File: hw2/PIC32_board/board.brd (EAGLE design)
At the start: 50 x 50 mm, 22 parts, among them J1 USB-MB-H

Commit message: Complete board design, add PCB gerber files.
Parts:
- removed V_REG(3.3V): MCP1702, me433:TO-92
- added U$1: SOT-223, me433:NU32V7_SOT223
- C1, C5: device me433:CT6032 -> me433:CAP-POL-0603
- C2, C3, C4, C7: device rcl:C1206 -> resistor:C0603
- CLOCK: value OSCO -> OSC; device me433:OSC -> me433:NU32V7_RESONATOR-SMD
- GREEN: value (none) -> GREEN; device led:LED3MM -> me433:LED-0603
- J1: value USB-MB-H -> USB; device me433:USB-MB-H -> me433:NU32V7_USB-MINIB
- R1, R2, R3, R4: device resistor:R1206 -> resistor:R0603
- RED: value (none) -> RED; device led:LED3MM -> me433:LED-0603
- RESET, USER: device me433:PUSH -> me433:NU32V7_MOM_SW
- moved SWITCH 44.3 mm to (47.6, 41.1), turned to 270 degrees
- moved CONN2 38.7 mm to (48.9, 16.5), turned to 90 degrees
- moved R1 37.7 mm to (48.3, 4.24), turned to 270 degrees
- moved R3 37.1 mm to (42.1, 42.2), turned to 0 degrees
- moved J1 36.3 mm to (6.49, 43.7), turned to 270 degrees
- moved C3 35.1 mm to (31.6, 38.0), turned to 270 degrees
- moved RED 35.1 mm to (38.0, 1.36), turned to 0 degrees
- moved R4 33.8 mm to (24.8, 43.4), turned to 0 degrees
- moved GREEN 33.6 mm to (31.8, 1.46), turned to 180 degrees
- moved RESET 32.8 mm to (39.6, 47.2), turned to 0 degrees
- moved CONN1 31.9 mm to (1.27, 34.3), turned to 270 degrees
- moved USER 28.0 mm to (29.4, 47.2)
- moved C4 23.6 mm to (31.4, 24.1), turned to 270 degrees
- moved PROGRAMMER 22.4 mm to (1.33, 12.1), turned to 270 degrees
- moved R2 21.0 mm to (26.5, 1.67)
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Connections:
- net N$7 renamed OSC2
- net N$8 renamed OSC1
- removed net N$3: C5.-, PIC.20
- removed net PGD\: PIC.4
- new net VCAP: C5.1, PIC.20
- net +3V3: now also C1.1, U$1.2; no longer C1.-, V_REG(3.3V).3
- net +5V: now also U$1.3, U$1.4; no longer V_REG(3.3V).2
- net B4/USER: now also USER.1.B; no longer USER.2
- net GND: now also C1.2, C5.2, PIC.8, RESET.2.A, U$1.1, USER.2.A; no longer C1.+, C5.+, RESET.1, USER.1, V_REG(3.3V).1
- net MCLR: now also RESET.1.B; no longer RESET.2
- net N$1: now also GREEN.C; no longer GREEN.K
- net N$2: now also RED.C; no longer RED.K
- net PGD: now also PIC.4
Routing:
- net +3V3: track 0.00 -> 146.8 mm, vias 0 -> 3
- net GND: track 0.00 -> 98.5 mm, vias 0 -> 4
- net MCLR: track 0.00 -> 74.2 mm, vias 0 -> 1
- net B4/USER: track 0.00 -> 65.1 mm, vias 0 -> 2
- net +5V: track 0.00 -> 52.2 mm, vias 0 -> 1
- net USBID: track 0.00 -> 47.0 mm, vias 0 -> 2
- net PGC: track 0.00 -> 46.9 mm, vias 0 -> 2
- net PGD: track 0.00 -> 45.5 mm, vias 0 -> 2
- net N$5: track 0.00 -> 44.4 mm
- net A4/LED: track 0.00 -> 42.2 mm, vias 0 -> 2
- net D+: track 0.00 -> 40.1 mm, vias 0 -> 2
- net D-: track 0.00 -> 36.9 mm, vias 0 -> 2
- net B9: track 0.00 -> 25.2 mm
- net B8: track 0.00 -> 25.2 mm
- net B7: track 0.00 -> 25.2 mm
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- added copper zone on layer 16, net GND
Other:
- board text added: "+3V3"
- board text added: "+5V"
- board text added: "A0"
- board text added: "A1"
- board text added: "A4/LED"
- board text added: "AAMIR HUSAIN"
- board text added: "B13"
- board text added: "B14"
- board text added: "B15"
- board text added: "B2"
- board text added: "B3"
- board text added: "B4/USER"
- board text added: "B7"
- board text added: "B8"
- board text added: "B9"
- board text added: "GND"
- board text added: "ME 433: Advanced Mechatronics"
- board text added: "PICKIT3"
- board text added: "Spring 2018"

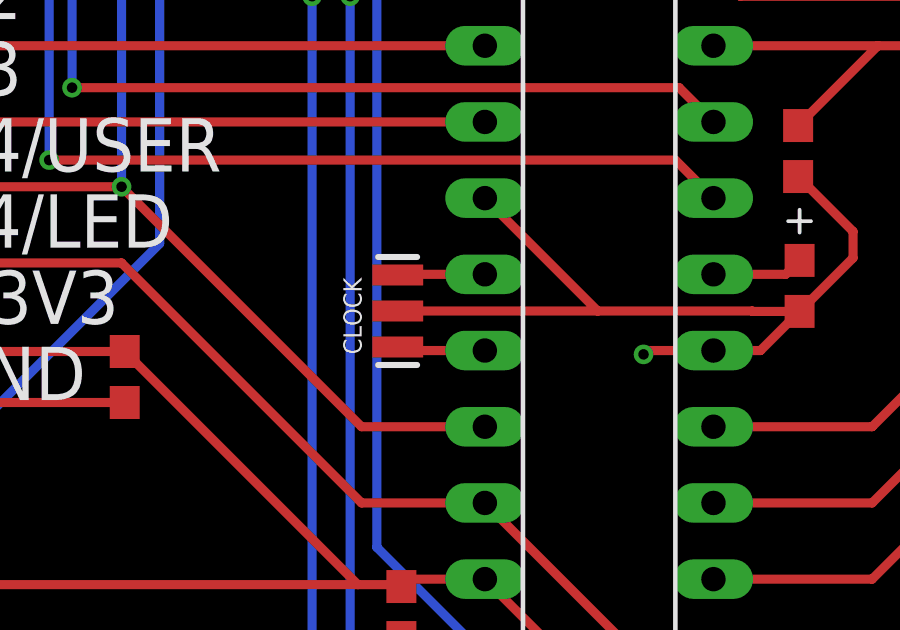
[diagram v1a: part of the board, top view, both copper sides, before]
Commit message: Move clock further from PIC
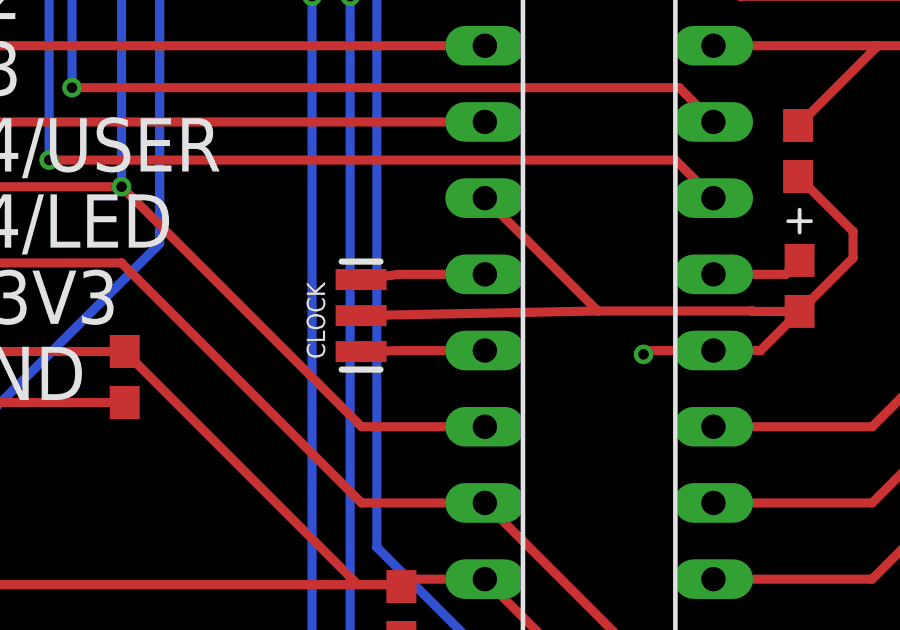
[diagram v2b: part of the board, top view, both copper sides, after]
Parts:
- moved CLOCK 1.23 mm to (16.9, 18.6)
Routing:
- net OSC1: track 2.92 -> 4.14 mm
- net GND: track 98.5 -> 99.8 mm
- net OSC2: track 2.95 -> 4.13 mm
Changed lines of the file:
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@@
 <layer number="155" name="FabDoc3" color="7" fill="1" visible="no" active="yes"/>
 <layer number="199" name="Contour" color="7" fill="1" visible="no" active="yes"/>
-<layer number="200" name="200bmp" color="1" fill="10" visible="yes" active="yes"/>
+<layer number="200" name="200bmp" color="1" fill="10" visible="no" active="yes"/>
 <layer number="201" name="201bmp" color="2" fill="10" visible="no" active="yes"/>
 <layer number="202" name="202bmp" color="3" fill="10" visible="no" active="yes"/>
@@
 <attribute name="VALUE" x="15.677" y="10.334" size="1.27" layer="27" rot="R270"/>
 </element>
-<element name="CLOCK" library="me433" package="NU32V7_RESONATOR-SMD" value="OSC" x="18.094" y="18.718" smashed="yes" rot="R270">
-<attribute name="NAME" x="16.2843" y="19.8293" size="0.6096" layer="25" rot="R270"/>
+<element name="CLOCK" library="me433" package="NU32V7_RESONATOR-SMD" value="OSC" x="16.8748" y="18.5656" smashed="yes" rot="R270">
+<attribute name="NAME" x="15.0651" y="19.6769" size="0.6096" layer="25" rot="R270"/>
 </element>
 <element name="CONN1" library="me433" package="1X08" value="" x="1.27" y="34.29" smashed="yes" rot="R270">
@@
 <wire x1="29.167" y1="37.173" x2="28.62" y2="37.72" width="0.3048" layer="1"/>
 <wire x1="29.924" y1="18.704" x2="31.491" y2="18.704" width="0.3048" layer="1"/>
-<wire x1="18.094" y1="18.718" x2="24.762" y2="18.718" width="0.3048" layer="1"/>
+<wire x1="16.8748" y1="18.5656" x2="24.762" y2="18.718" width="0.3048" layer="1"/>
 <wire x1="24.762" y1="18.718" x2="29.91" y2="18.718" width="0.3048" layer="1"/>
 <wire x1="31.491" y1="18.704" x2="33.273" y2="20.486" width="0.3048" layer="1"/>
@@
 <contactref element="PIC" pad="10"/>
 <wire x1="21" y1="17.4" x2="18.212" y2="17.4" width="0.3048" layer="1"/>
-<wire x1="18.212" y1="17.4" x2="18.094" y2="17.518" width="0.3048" layer="1"/>
+<wire x1="18.212" y1="17.4" x2="16.8748" y2="17.3656" width="0.3048" layer="1"/>
 </signal>
 <signal name="OSC1">
@@
 <contactref element="PIC" pad="9"/>
 <wire x1="21" y1="19.94" x2="18.116" y2="19.94" width="0.3048" layer="1"/>
-<wire x1="18.116" y1="19.94" x2="18.094" y2="19.918" width="0.3048" layer="1"/>
+<wire x1="18.116" y1="19.94" x2="16.8748" y2="19.7656" width="0.3048" layer="1"/>
 </signal>
 <signal name="B4/USER">
